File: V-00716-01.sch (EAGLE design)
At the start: 24 parts, among them Q1 16MHz, U1 ATMEGA32-16AU, U2 ATMEGA32U2-AU, X1 MINI-USB-32005-201

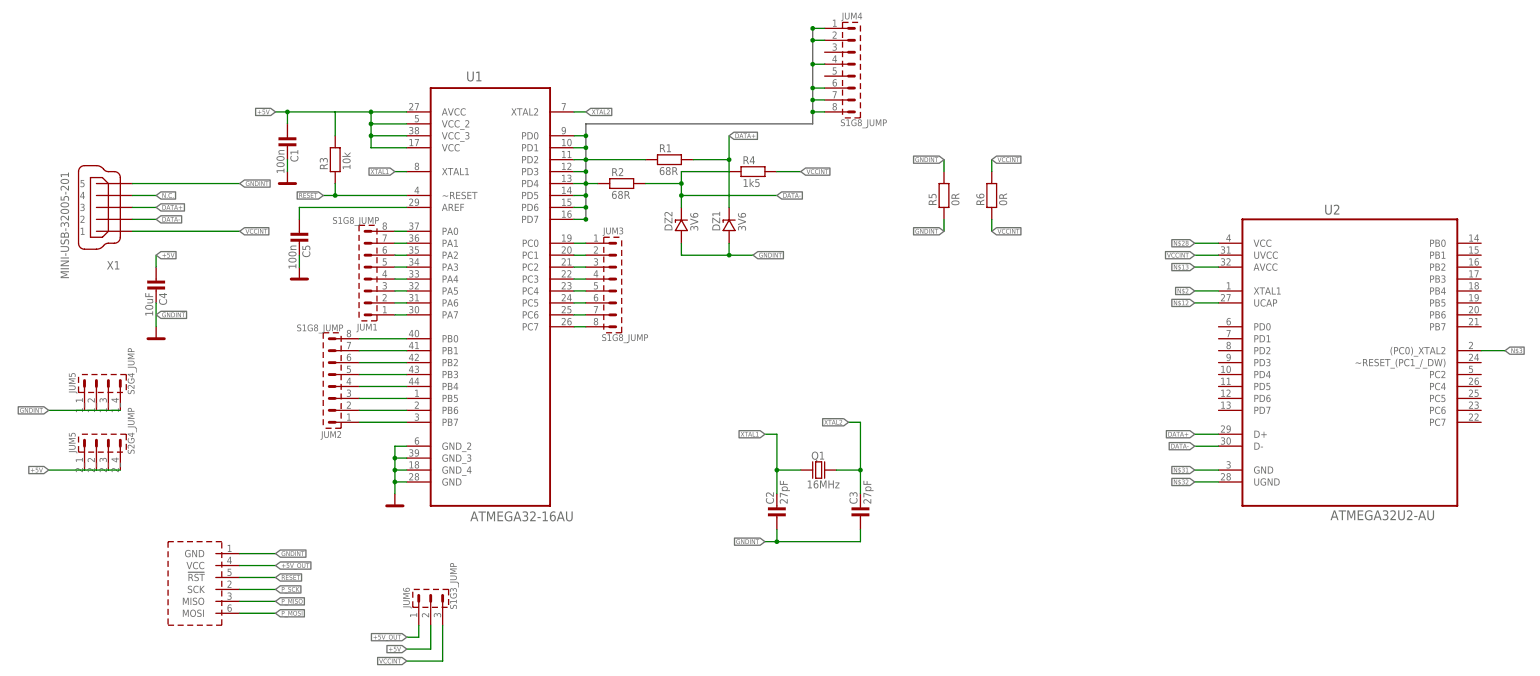
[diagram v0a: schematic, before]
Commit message: v.2.0.0
Nová verze z jiným mcu atmega32u2
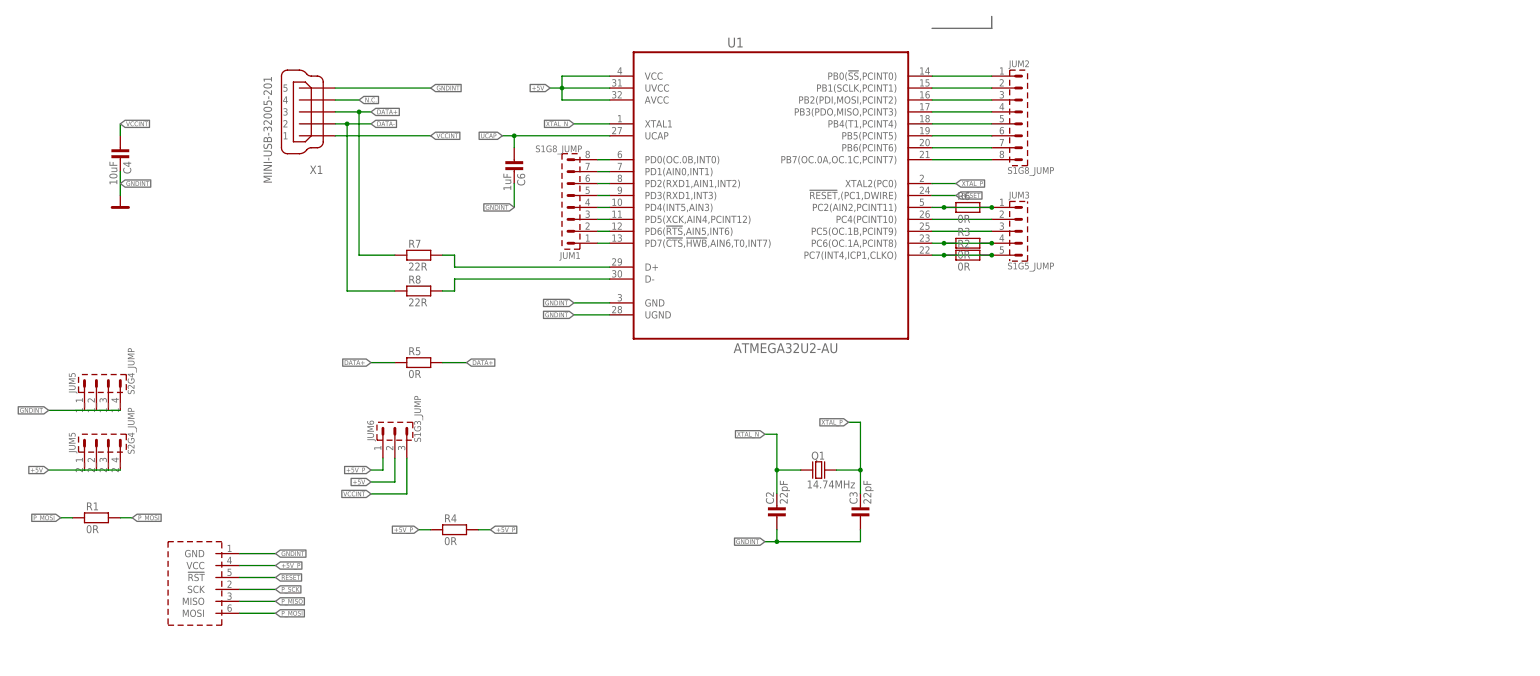
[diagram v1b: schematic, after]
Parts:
- removed C1, C5: 100n, #PaJa_31:C-KER_1206
- removed DZ1, DZ2: 3V6, #PaJa_31:D-BZV55C_SMD_0,5W-ZENER
- removed JUM4: S1G8_JUMP, #PaJa_konektory:S1G8_JUMP
- removed U2: ATMEGA32U2-AU, #_Atmel_By_element14_Batch_1-00:ATMEGA32U2-AU
- added C6: 1uF, #PaJa_31:C-KER_1206
- added R7, R8: 22R, #PaJa_31:R_1206
- C2, C3: value 27pF -> 22pF
- JUM3: value S1G8_JUMP -> S1G5_JUMP; device #PaJa_konektory:S1G8_JUMP -> #PaJa_konektory:S1G5_JUMP
- Q1: value 16MHz -> 14.74MHz
- R1, R2: value 68R -> 0R
- R3: value 10k -> 0R
- R4: value 1k5 -> 0R
- U1: value ATMEGA32-16AU -> ATMEGA32U2-AU; device #_Atmel_By_element14_Batch_1-00:ATMEGA32-16AU -> #_Atmel_By_element14_Batch_1-00:ATMEGA32U2-AU
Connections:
- net XTAL1 renamed XTAL_N
- removed net +5V_OUT: JUM6.1, U$1.VCC
- removed net N$17: JUM2.6, U1.PB2
- removed net N$18: JUM2.7, U1.PB1
- removed net N$19: JUM2.8, U1.PB0
- removed net N$24: JUM3.5, U1.PC4
- removed net N$25: JUM3.6, U1.PC5
- removed net N$26: JUM3.7, U1.PC6
- removed net N$27: JUM3.8, U1.PC7
- removed net N$28: U2.VCC
- removed net N$31: U2.GND
- removed net N$32: U2.UGND
- removed net PD0: JUM4.1, U1.PD0
- removed net PD1: JUM4.2, U1.PD1
- removed net PD2: R1.1, U1.PD2
- removed net PD3: JUM4.4, U1.PD3
- removed net PD4: R2.1, U1.PD4
- removed net PD5: JUM4.6, U1.PD5
- removed net PD6: JUM4.7, U1.PD6
- removed net PD7: JUM4.8, U1.PD7
- removed net XTAL2: C3.2, Q1.2, U1.XTAL2
- new net +5V_P: JUM6.1, R4.1, R4.2, U$1.VCC
- new net N$14: JUM3.4, R3.1, R3.2, U1.PC6(OC.1A,PCINT8)
- new net UCAP: C6.1, U1.UCAP
- new net XTAL_P: C3.2, Q1.2, U1.XTAL2(PC0)
- net +5V: now also U1.UVCC; no longer C1.1, C4.1, R3.2, U1.VCC_2, U1.VCC_3
- net DATA+: now also R5.1, R5.2, R7.1; no longer DZ1.K, R1.2, U2.D+
- net DATA-: now also R8.1; no longer DZ2.K, R2.2, R4.1, U2.D-
- net GNDINT: now also C6.2, U1.UGND; no longer C1.2, C5.2, DZ1.A, DZ2.A, R5.1, R5.2, U1.GND_2, U1.GND_3, U1.GND_4
- net N$1: now also JUM1.1, U1.PD7(!CTS,!HWB,AIN6,T0,INT7); no longer C5.1, U1.AREF
- net N$10: now also JUM3.1, R6.1, R6.2, U1.PC2(AIN2,PCINT11); no longer JUM1.7, U1.PA1
- net N$11: now also JUM3.2, U1.PC4(PCINT10); no longer JUM1.8, U1.PA0
- net N$12: now also R8.2, U1.D-; no longer U2.UCAP
- net N$13: now also JUM3.3, U1.PC5(OC.1B,PCINT9); no longer U2.AVCC
- net N$15: now also JUM3.5, R2.1, R2.2, U1.PC7(INT4,ICP1,CLKO); no longer JUM2.4, U1.PB4
- net N$16: now also JUM2.1, U1.PB0(!SS,PCINT0); no longer JUM2.5, U1.PB3
- net N$2: now also R7.2, U1.D+; no longer U2.XTAL1
- net N$20: now also JUM2.5, U1.PB4(T1,PCINT4); no longer JUM3.1, U1.PC0
- net N$21: now also JUM2.6, U1.PB5(PCINT5); no longer JUM3.2, U1.PC1
- net N$22: now also JUM2.7, U1.PB6(PCINT6); no longer JUM3.3, U1.PC2
- net N$23: now also JUM2.8, U1.PB7(OC.0A,OC.1C,PCINT7); no longer JUM3.4, U1.PC3
- net N$3: now also JUM1.2, U1.PD6(!RTS,AIN5,INT6); no longer U2.(PC0)_XTAL2
- net N$4: now also JUM1.3, U1.PD5(XCK,AIN4,PCINT12); no longer JUM1.1, U1.PA7
- net N$5: now also JUM1.4, U1.PD4(INT5,AIN3); no longer JUM1.2, U1.PA6
- net N$6: now also JUM1.5, U1.PD3(RXD1,INT3); no longer JUM1.3, U1.PA5
- net N$7: now also JUM1.6, U1.PD2(RXD1,AIN1,INT2); no longer JUM1.4, U1.PA4
- net N$8: now also JUM1.7, U1.PD1(AIN0,INT1); no longer JUM1.5, U1.PA3
- net N$9: now also JUM1.8, U1.PD0(OC.0B,INT0); no longer JUM1.6, U1.PA2
- net P_MISO: now also JUM2.4, U1.PB3(PDO,MISO,PCINT3); no longer JUM2.2, U1.PB6
- net P_MOSI: now also R1.1, R1.2, U1.PB2(PDI,MOSI,PCINT2); no longer U1.PB5
- net P_SCK: now also JUM2.2, U1.PB1(SCLK,PCINT1); no longer JUM2.1, U1.PB7
- net RESET: now also U1.!RESET,(PC1,DWIRE); no longer R3.1, U1.~RESET
- net VCCINT: now also C4.1; no longer R4.2, R6.1, R6.2, U2.UVCC
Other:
- moved on the sheet: C4, JUM1, JUM2, JUM6, R1, R2, R3, R4, R5, R6, X1
